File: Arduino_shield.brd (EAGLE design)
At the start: 98.7 x 73.6 mm, 7 parts, among them X1 6PIN_CON

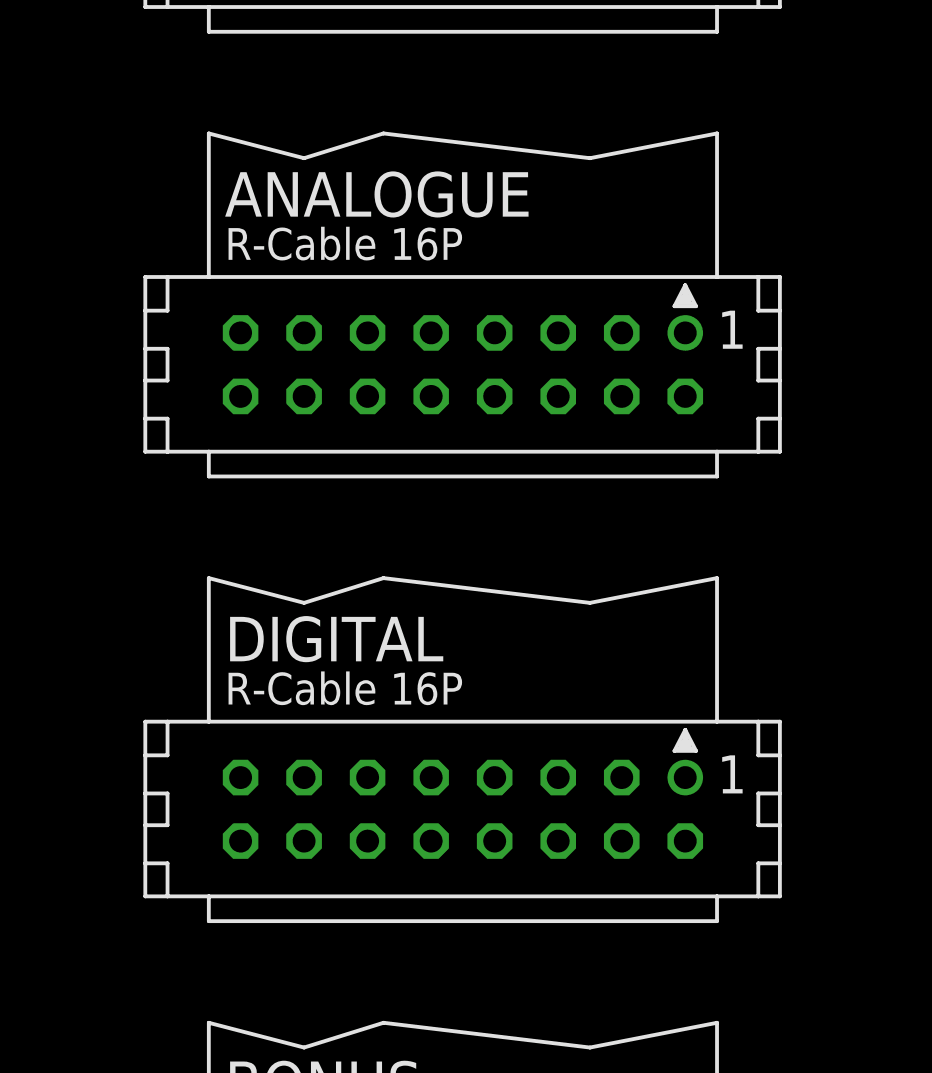
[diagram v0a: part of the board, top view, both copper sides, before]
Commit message: Official_flat_cable_connections
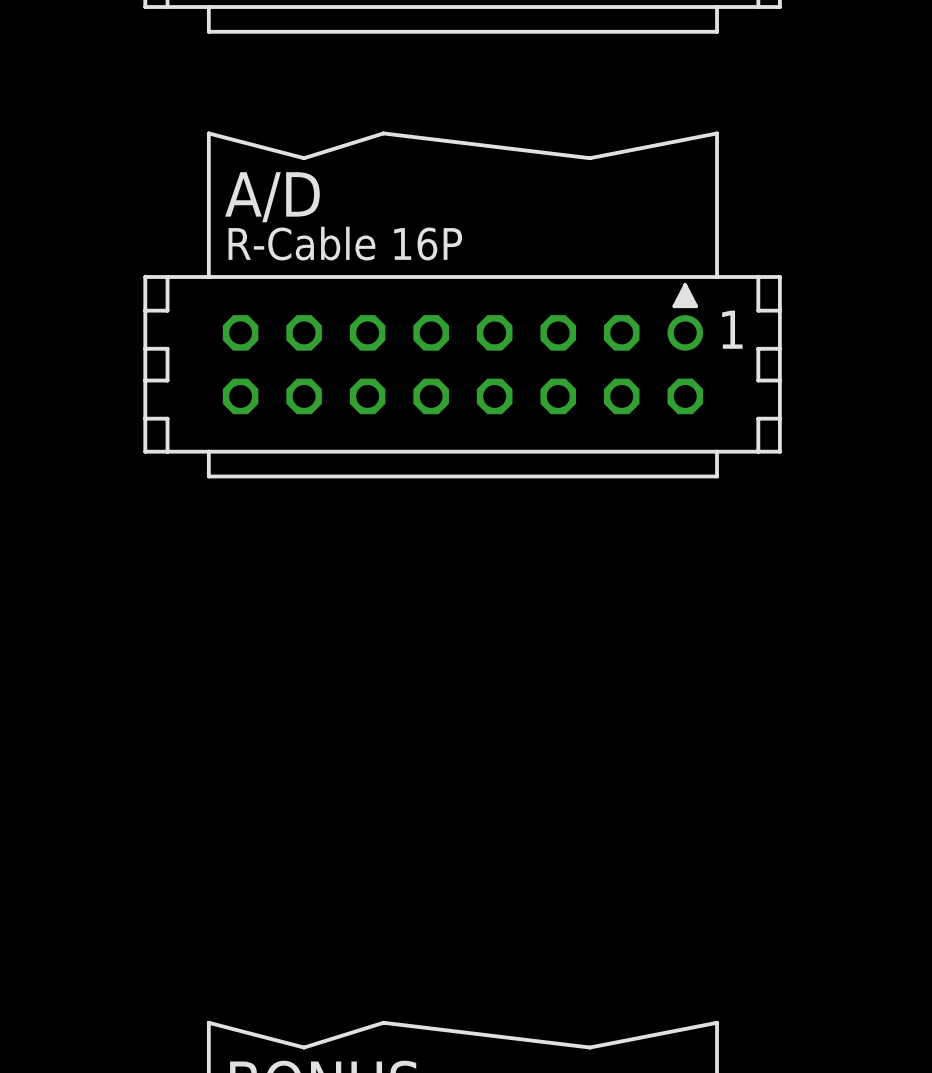
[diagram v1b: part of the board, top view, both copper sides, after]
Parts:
- removed DIGITAL: (no value), con-harting:CON16L
- renumbered ANALOGUE to A/D
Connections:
- new net MISO: A/D.3, BONUS.3, TEMP1.3, TEMP2.3, U$1.MISO_ICSP
- net +15V: no longer DIGITAL.14
- net +3V3: no longer DIGITAL.12
- net +5V: no longer DIGITAL.1
- net -15V: no longer DIGITAL.16
- net DOUT: now also A/D.10; no longer DIGITAL.8
- net GND: no longer DIGITAL.15
- net MOSI: no longer DIGITAL.4
- net SCK: no longer DIGITAL.6
- net SCL: no longer DIGITAL.5
- net SDA: no longer DIGITAL.7
- net SS4: no longer DIGITAL.2
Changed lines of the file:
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@@
 <attribute name="MF" value="" x="7.62" y="-128.27" size="1.778" layer="27" display="off"/>
 </element>
-<element name="ANALOGUE" library="con-harting" package="CON16L" value="" x="7.62" y="-146.05">
+<element name="A/D" library="con-harting" package="CON16L" value="" x="7.62" y="-146.05">
 <attribute name="OC_FARNELL" value="unknown" x="7.62" y="-146.05" size="1.778" layer="27" display="off"/>
 <attribute name="MPN" value="" x="7.62" y="-146.05" size="1.778" layer="27" display="off"/>
 <attribute name="OC_NEWARK" value="unknown" x="7.62" y="-146.05" size="1.778" layer="27" display="off"/>
 <attribute name="MF" value="" x="7.62" y="-146.05" size="1.778" layer="27" display="off"/>
-</element>
-<element name="DIGITAL" library="con-harting" package="CON16L" value="" x="7.62" y="-163.83">
-<attribute name="OC_FARNELL" value="unknown" x="7.62" y="-163.83" size="1.778" layer="27" display="off"/>
-<attribute name="MPN" value="" x="7.62" y="-163.83" size="1.778" layer="27" display="off"/>
-<attribute name="OC_NEWARK" value="unknown" x="7.62" y="-163.83" size="1.778" layer="27" display="off"/>
-<attribute name="MF" value="" x="7.62" y="-163.83" size="1.778" layer="27" display="off"/>
 </element>
 <element name="BONUS" library="con-harting" package="CON16L" value="" x="7.62" y="-181.61">
@@
 <contactref element="TEMP1" pad="12"/>
 <contactref element="TEMP2" pad="12"/>
-<contactref element="ANALOGUE" pad="12"/>
-<contactref element="DIGITAL" pad="12"/>
+<contactref element="A/D" pad="12"/>
 <contactref element="BONUS" pad="12"/>
-<wire x1="3.81" y1="-165.1" x2="3.81" y2="-182.88" width="0" layer="19" extent="1-1"/>
-<wire x1="3.81" y1="-147.32" x2="3.81" y2="-165.1" width="0" layer="19" extent="1-1"/>
+<wire x1="3.81" y1="-147.32" x2="3.81" y2="-182.88" width="0" layer="19" extent="1-1"/>
 <wire x1="3.81" y1="-129.54" x2="3.81" y2="-147.32" width="0" layer="19" extent="1-1"/>
 <wire x1="3.81" y1="-16.51" x2="3.81" y2="-129.54" width="0" layer="19" extent="1-1"/>
@@
 <contactref element="TEMP1" pad="14"/>
 <contactref element="TEMP2" pad="14"/>
-<contactref element="ANALOGUE" pad="14"/>
-<contactref element="DIGITAL" pad="14"/>
+<contactref element="A/D" pad="14"/>
 <contactref element="BONUS" pad="14"/>
-<wire x1="1.27" y1="-165.1" x2="1.27" y2="-182.88" width="0" layer="19" extent="1-1"/>
-<wire x1="1.27" y1="-147.32" x2="1.27" y2="-165.1" width="0" layer="19" extent="1-1"/>
+<wire x1="1.27" y1="-147.32" x2="1.27" y2="-182.88" width="0" layer="19" extent="1-1"/>
 <wire x1="1.27" y1="-129.54" x2="1.27" y2="-147.32" width="0" layer="19" extent="1-1"/>
 <wire x1="2.54" y1="-106.68" x2="1.27" y2="-129.54" width="0" layer="19" extent="1-1"/>
@@
 <contactref element="TEMP1" pad="16"/>
 <contactref element="TEMP2" pad="16"/>
-<contactref element="ANALOGUE" pad="16"/>
-<contactref element="DIGITAL" pad="16"/>
+<contactref element="A/D" pad="16"/>
 <contactref element="BONUS" pad="16"/>
-<wire x1="-1.27" y1="-165.1" x2="-1.27" y2="-182.88" width="0" layer="19" extent="1-1"/>
-<wire x1="-1.27" y1="-147.32" x2="-1.27" y2="-165.1" width="0" layer="19" extent="1-1"/>
+<wire x1="-1.27" y1="-147.32" x2="-1.27" y2="-182.88" width="0" layer="19" extent="1-1"/>
 <wire x1="-1.27" y1="-129.54" x2="-1.27" y2="-147.32" width="0" layer="19" extent="1-1"/>
 <wire x1="7.54" y1="-106.68" x2="-1.27" y2="-129.54" width="0" layer="19" extent="1-1"/>
@@
 <contactref element="TEMP1" pad="1"/>
 <contactref element="TEMP2" pad="1"/>
-<contactref element="ANALOGUE" pad="1"/>
-<contactref element="DIGITAL" pad="1"/>
+<contactref element="A/D" pad="1"/>
 <contactref element="BONUS" pad="1"/>
-<wire x1="16.51" y1="-162.56" x2="16.51" y2="-180.34" width="0" layer="19" extent="1-1"/>
-<wire x1="16.51" y1="-144.78" x2="16.51" y2="-162.56" width="0" layer="19" extent="1-1"/>
+<wire x1="16.51" y1="-144.78" x2="16.51" y2="-180.34" width="0" layer="19" extent="1-1"/>
 <wire x1="16.51" y1="-127" x2="16.51" y2="-144.78" width="0" layer="19" extent="1-1"/>
 <wire x1="12.54" y1="-106.68" x2="16.51" y2="-127" width="0" layer="19" extent="1-1"/>
@@
 <contactref element="TEMP1" pad="15"/>
 <contactref element="TEMP2" pad="15"/>
-<contactref element="ANALOGUE" pad="15"/>
-<contactref element="DIGITAL" pad="15"/>
+<contactref element="A/D" pad="15"/>
 <contactref element="BONUS" pad="15"/>
 <contactref element="U$1" pad="GND_1"/>
-<wire x1="-1.27" y1="-162.56" x2="-1.27" y2="-180.34" width="0" layer="19" extent="1-1"/>
-<wire x1="-1.27" y1="-144.78" x2="-1.27" y2="-162.56" width="0" layer="19" extent="1-1"/>
+<wire x1="-1.27" y1="-144.78" x2="-1.27" y2="-180.34" width="0" layer="19" extent="1-1"/>
 <wire x1="-1.27" y1="-127" x2="-1.27" y2="-144.78" width="0" layer="19" extent="1-1"/>
 <wire x1="17.54" y1="-106.68" x2="-1.27" y2="-127" width="0" layer="19" extent="1-1"/>
@@
 <contactref element="TEMP1" pad="7"/>
 <contactref element="TEMP2" pad="7"/>
-<contactref element="ANALOGUE" pad="7"/>
-<contactref element="DIGITAL" pad="7"/>
+<contactref element="A/D" pad="7"/>
 <contactref element="BONUS" pad="7"/>
-<wire x1="8.89" y1="-162.56" x2="8.89" y2="-180.34" width="0" layer="19" extent="1-1"/>
-<wire x1="8.89" y1="-144.78" x2="8.89" y2="-162.56" width="0" layer="19" extent="1-1"/>
+<wire x1="8.89" y1="-144.78" x2="8.89" y2="-180.34" width="0" layer="19" extent="1-1"/>
 <wire x1="8.89" y1="-127" x2="8.89" y2="-144.78" width="0" layer="19" extent="1-1"/>
 <wire x1="8.89" y1="-13.97" x2="8.89" y2="-127" width="0" layer="19" extent="1-1"/>
@@
 <contactref element="TEMP1" pad="5"/>
 <contactref element="TEMP2" pad="5"/>
-<contactref element="ANALOGUE" pad="5"/>
-<contactref element="DIGITAL" pad="5"/>
+<contactref element="A/D" pad="5"/>
 <contactref element="BONUS" pad="5"/>
-<wire x1="11.43" y1="-162.56" x2="11.43" y2="-180.34" width="0" layer="19" extent="1-1"/>
-<wire x1="11.43" y1="-144.78" x2="11.43" y2="-162.56" width="0" layer="19" extent="1-1"/>
+<wire x1="11.43" y1="-144.78" x2="11.43" y2="-180.34" width="0" layer="19" extent="1-1"/>
 <wire x1="11.43" y1="-127" x2="11.43" y2="-144.78" width="0" layer="19" extent="1-1"/>
 <wire x1="11.43" y1="-13.97" x2="11.43" y2="-127" width="0" layer="19" extent="1-1"/>
@@
 <contactref element="TEMP1" pad="4"/>
 <contactref element="TEMP2" pad="4"/>
-<contactref element="ANALOGUE" pad="4"/>
-<contactref element="DIGITAL" pad="4"/>
+<contactref element="A/D" pad="4"/>
 <contactref element="BONUS" pad="4"/>
-<wire x1="13.97" y1="-165.1" x2="13.97" y2="-182.88" width="0" layer="19" extent="1-1"/>
-<wire x1="13.97" y1="-147.32" x2="13.97" y2="-165.1" width="0" layer="19" extent="1-1"/>
+<wire x1="13.97" y1="-147.32" x2="13.97" y2="-182.88" width="0" layer="19" extent="1-1"/>
 <wire x1="13.97" y1="-129.54" x2="13.97" y2="-147.32" width="0" layer="19" extent="1-1"/>
 <wire x1="13.97" y1="-16.51" x2="13.97" y2="-129.54" width="0" layer="19" extent="1-1"/>
@@
 <contactref element="TEMP1" pad="6"/>
 <contactref element="TEMP2" pad="6"/>
-<contactref element="ANALOGUE" pad="6"/>
-<contactref element="DIGITAL" pad="6"/>
+<contactref element="A/D" pad="6"/>
 <contactref element="BONUS" pad="6"/>
-<wire x1="11.43" y1="-165.1" x2="11.43" y2="-182.88" width="0" layer="19" extent="1-1"/>
-<wire x1="11.43" y1="-147.32" x2="11.43" y2="-165.1" width="0" layer="19" extent="1-1"/>
+<wire x1="11.43" y1="-147.32" x2="11.43" y2="-182.88" width="0" layer="19" extent="1-1"/>
 <wire x1="11.43" y1="-129.54" x2="11.43" y2="-147.32" width="0" layer="19" extent="1-1"/>
 <wire x1="11.43" y1="-16.51" x2="11.43" y2="-129.54" width="0" layer="19" extent="1-1"/>
@@
 <signal name="SS3">
 <contactref element="U$1" pad="4"/>
-<contactref element="ANALOGUE" pad="2"/>
+<contactref element="A/D" pad="2"/>
 <wire x1="34.29" y1="54.61" x2="16.51" y2="-147.32" width="0" layer="19" extent="1-1"/>
 </signal>
 <signal name="SS4">
 <contactref element="U$1" pad="5"/>
-<contactref element="DIGITAL" pad="2"/>
-<wire x1="31.75" y1="54.61" x2="16.51" y2="-165.1" width="0" layer="19" extent="1-1"/>
 </signal>
 <signal name="SS5">
@@
 <signal name="AOUT">
 <contactref element="U$1" pad="A3"/>
-<contactref element="ANALOGUE" pad="8"/>
+<contactref element="A/D" pad="8"/>
 <wire x1="39.37" y1="6.35" x2="8.89" y2="-147.32" width="0" layer="19" extent="1-1"/>
 </signal>
 <signal name="DOUT">
-<contactref element="DIGITAL" pad="8"/>
 <contactref element="U$1" pad="9"/>
-<wire x1="20.32" y1="54.61" x2="8.89" y2="-165.1" width="0" layer="19" extent="1-1"/>
+<contactref element="A/D" pad="10"/>
+<wire x1="20.32" y1="54.61" x2="6.35" y2="-147.32" width="0" layer="19" extent="1-1"/>
 </signal>
 <signal name="BAOUT">
@@
 <wire x1="17.78" y1="54.61" x2="6.35" y2="-182.88" width="0" layer="19" extent="1-1"/>
 </signal>
+<signal name="MISO">
+<contactref element="U$1" pad="MISO_ICSP"/>
+<contactref element="TEMP1" pad="3"/>
+<contactref element="TEMP2" pad="3"/>
+<contactref element="A/D" pad="3"/>
+<contactref element="BONUS" pad="3"/>
+<wire x1="13.97" y1="-144.78" x2="13.97" y2="-180.34" width="0" layer="19" extent="1-1"/>
+<wire x1="13.97" y1="-127" x2="13.97" y2="-144.78" width="0" layer="19" extent="1-1"/>
+<wire x1="13.97" y1="-13.97" x2="13.97" y2="-127" width="0" layer="19" extent="1-1"/>
+<wire x1="44.45" y1="34.29" x2="13.97" y2="-13.97" width="0" layer="19" extent="1-1"/>
+</signal>
 </signals>

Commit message: Added_relays
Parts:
- added DEV1, DEV2, DEV3, DEV4, DEV5, DEV6, DEV7, DEV8: SMA-F_A0201, 1AKarstenLib:SMA-F_A0201
- added REL1, REL2, REL3, REL4: TE_2-1462039-6TE_2-1462039-6_0_0, TE - 2-1462039-6:TE_2-1462039-6_0
- renumbered X1 to PWR
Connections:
- new net D1A: DEV1.1, REL2.6
- new net D1B: DEV1.2, DEV1.3, DEV1.4, DEV1.5, REL2.7
- new net D2A: DEV2.1, REL2.3
- new net D2B: DEV2.2, DEV2.3, DEV2.4, DEV2.5, REL2.2
- new net D3A: DEV3.1
- new net D3B: DEV3.2, DEV3.3, DEV3.4, DEV3.5
- new net D4A: DEV4.1, REL1.6
- new net D4B: DEV4.2, DEV4.3, DEV4.4, DEV4.5, REL1.7
- new net D5A: DEV5.1, REL1.3, REL4.6
- new net D5B: DEV5.2, DEV5.3, DEV5.4, DEV5.5, REL1.2, REL4.7
- new net D6A: DEV6.1, REL4.3
- new net D6B: DEV6.2, DEV6.3, DEV6.4, DEV6.5, REL4.2
- new net D7A: DEV7.1, REL3.6
- new net D7B: DEV7.2, DEV7.3, DEV7.4, DEV7.5, REL3.7
- new net D8A: DEV8.1, REL3.3
- new net D8B: DEV8.2, DEV8.3, DEV8.4, DEV8.5, REL3.2
- new net RR1: REL1.1, U$1.10
- new net RR2: REL2.1, U$1.11
- new net RR3: REL3.1, U$1.12
- new net RR4: REL4.1, U$1.13
- net BDOUT: now also U$1.9; no longer U$1.10
- net DOUT: now also U$1.8; no longer U$1.9
- net GND: now also REL1.8, REL2.8, REL3.8, REL4.8

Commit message: Final_v1
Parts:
- added BUZZER: 3PIN_CON, CoilCircuitLibrary_E7:3PIN_CON
- added EXTRAANALOGUE, EXTRADIG: (no value), pinhead:2X16
- DEV1, DEV2, DEV3, DEV4, DEV5, DEV6, DEV7, DEV8: value SMA-F_A0201 -> 3PIN_CON; device 1AKarstenLib:SMA-F_A0201 -> CoilCircuitLibrary_E7:3PIN_CON
- moved DEV1 307.4 mm to (-20.3, -607.1)
- moved DEV2 298.5 mm to (-20.3, -629.9)
- moved DEV3 289.6 mm to (-20.3, -652.8)
- moved DEV4 280.7 mm to (-20.3, -675.6)
- moved DEV5 271.8 mm to (-20.3, -698.5)
- moved DEV6 262.9 mm to (-20.3, -721.4)
- moved DEV7 254.0 mm to (-20.3, -744.2)
- moved DEV8 245.1 mm to (-20.3, -767.1)
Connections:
- new net BUZZ: BUZZER.P$2, U$1.7
- new net D22: EXTRADIG.1, U$1.22
- new net D23: EXTRADIG.2, U$1.23
- new net D24: EXTRADIG.3, U$1.24
- new net D25: EXTRADIG.4, U$1.25
- new net D26: EXTRADIG.5, U$1.26
- new net D27: EXTRADIG.6, U$1.27
- new net D28: EXTRADIG.7, U$1.28
- new net D29: EXTRADIG.8, U$1.29
- new net D30: EXTRADIG.9, U$1.30
- new net D31: EXTRADIG.10, U$1.31
- new net D32: EXTRADIG.11, U$1.32
- new net D33: EXTRADIG.12, U$1.33
- new net D34: EXTRADIG.13, U$1.34
- new net D35: EXTRADIG.14, U$1.35
- new net D36: EXTRADIG.15, U$1.36
- new net D37: EXTRADIG.16, U$1.37
- new net D38: EXTRADIG.17, U$1.38
- new net D39: EXTRADIG.18, U$1.39
- new net D40: EXTRADIG.19, U$1.40
- new net D41: EXTRADIG.20, U$1.41
- new net D42: EXTRADIG.21, U$1.42
- new net D43: EXTRADIG.22, U$1.43
- new net D44: EXTRADIG.23, U$1.44
- new net D45: EXTRADIG.24, U$1.45
- new net D46: EXTRADIG.25, U$1.46
- new net D47: EXTRADIG.26, U$1.47
- new net D48: EXTRADIG.27, U$1.48
- new net D49: EXTRADIG.28, U$1.49
- new net D50: EXTRADIG.29, U$1.50
- new net D51: EXTRADIG.30, U$1.51
- new net D52: EXTRADIG.31, U$1.52
- new net D53: EXTRADIG.32, U$1.53
- new net N$57: EXTRAANALOGUE.2, U$1.A4
- new net N$58: EXTRAANALOGUE.4, U$1.A5
- new net N$59: EXTRAANALOGUE.6, U$1.A6
- new net N$60: EXTRAANALOGUE.8, U$1.A7
- new net N$61: EXTRAANALOGUE.10, U$1.A8
- new net N$62: EXTRAANALOGUE.12, U$1.A9
- new net N$63: EXTRAANALOGUE.14, U$1.A10
- new net N$64: EXTRAANALOGUE.16, U$1.A11
- net +15V: now also EXTRAANALOGUE.1
- net +3V3: now also EXTRAANALOGUE.7
- net +5V: now also EXTRAANALOGUE.5
- net -15V: now also EXTRAANALOGUE.3
- net D1A: now also DEV1.P$3; no longer DEV1.1
- net D1B: now also DEV1.P$2; no longer DEV1.2, DEV1.3, DEV1.4, DEV1.5
- net D2A: now also DEV2.P$3; no longer DEV2.1
- net D2B: now also DEV2.P$2; no longer DEV2.2, DEV2.3, DEV2.4, DEV2.5
- net D3A: now also DEV3.P$3, REL1.6; no longer DEV3.1
- net D3B: now also DEV3.P$2, REL1.7; no longer DEV3.2, DEV3.3, DEV3.4, DEV3.5
- net D4A: now also DEV4.P$3, REL1.3; no longer DEV4.1, REL1.6
- net D4B: now also DEV4.P$2, REL1.2; no longer DEV4.2, DEV4.3, DEV4.4, DEV4.5, REL1.7
- net D5A: now also DEV5.P$3; no longer DEV5.1, REL1.3
- net D5B: now also DEV5.P$2; no longer DEV5.2, DEV5.3, DEV5.4, DEV5.5, REL1.2
- net D6A: now also DEV6.P$3; no longer DEV6.1
- net D6B: now also DEV6.P$2; no longer DEV6.2, DEV6.3, DEV6.4, DEV6.5
- net D7A: now also DEV7.P$3; no longer DEV7.1
- net D7B: now also DEV7.P$2; no longer DEV7.2, DEV7.3, DEV7.4, DEV7.5
- net D8A: now also DEV8.P$3; no longer DEV8.1
- net D8B: now also DEV8.P$2; no longer DEV8.2, DEV8.3, DEV8.4, DEV8.5
- net GND: now also BUZZER.P$3, EXTRAANALOGUE.9

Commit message: Board_init
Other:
- board size 98.7 x 73.6 mm -> 240 x 880 mm
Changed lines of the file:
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@@
 <setting verticaltext="up"/>
 </settings>
-<grid distance="0.05" unitdist="inch" unit="inch" style="lines" multiple="1" display="yes" altdistance="0.025" altunitdist="inch" altunit="inch"/>
+<grid distance="40" unitdist="mm" unit="mm" style="lines" multiple="1" display="yes" altdistance="1" altunitdist="mm" altunit="mm"/>
 <layers>
 <layer number="1" name="Top" color="4" fill="1" visible="yes" active="yes"/>
@@
 <board>
 <plain>
-<wire x1="-8.89" y1="-5.08" x2="89.84" y2="-5.08" width="0" layer="20"/>
-<wire x1="89.84" y1="-5.08" x2="89.84" y2="68.57" width="0" layer="20"/>
-<wire x1="89.84" y1="68.57" x2="-8.89" y2="68.57" width="0" layer="20"/>
-<wire x1="-8.89" y1="68.57" x2="-8.89" y2="-5.08" width="0" layer="20"/>
+<wire x1="-120" y1="-800" x2="120" y2="-800.01" width="0" layer="20"/>
+<wire x1="120" y1="-800.01" x2="120" y2="80" width="0" layer="20"/>
+<wire x1="120" y1="80" x2="-120" y2="80.01" width="0" layer="20"/>
+<wire x1="-120" y1="80.01" x2="-120" y2="-800" width="0" layer="20"/>
 </plain>
 <attributes>
